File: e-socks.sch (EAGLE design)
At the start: 91 parts, among them IC1 CC2540, IC2 741G240DCK, IC3 TPS6300X, P2 TMAV433BAA, Q1 FA-20H(32MHz), Q2 ABS06, U2 MAX21000, X4 1296-T10

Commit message: erstes commit für diesen branch
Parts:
- removed C1: 100nF, rcl:C-EUC0402
- removed IC3: TPS6300X, m_vreg:TPS6300XDRC
- removed L1: CR32, inductors:CR32
- added LED3, LED4: Blue/2.9V@10mA, led:LEDCHIP-LED0603
- added R8: 47RR, rcl:R-EU_R0402
- C5, C6: value 10µF -> 22µF; device rcl:C-EUC0603 -> rcl:C-EUC0805
- R6: value 100R -> 47RR
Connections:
- removed net N$10: C1.2, IC3.!PS!/SYNC, IC3.VINA, R6.2
- net +5V: now also IC7.VOUT; no longer IC3.VOUT
- net 5V_ENABLE: now also IC7.EN; no longer IC3.EN
- net GND: now also LED3.C, LED4.C; no longer C1.1, IC3.GND, IC3.PGND
- net HEATER1_PWR: now also R8.1
- net HEATER2_PWR: now also R6.1
- net N$1: now also LED3.A, R6.2; no longer IC3.L1, L1.1
- net N$3: now also LED4.A, R8.2; no longer IC3.L2, L1.2
- net N$4: now also IC7.FB; no longer IC3.FB
- net VBAT: no longer IC3.VIN, R6.1
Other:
- moved on the sheet: C5, C6, C9, IC7, L3, R3, R5, R6

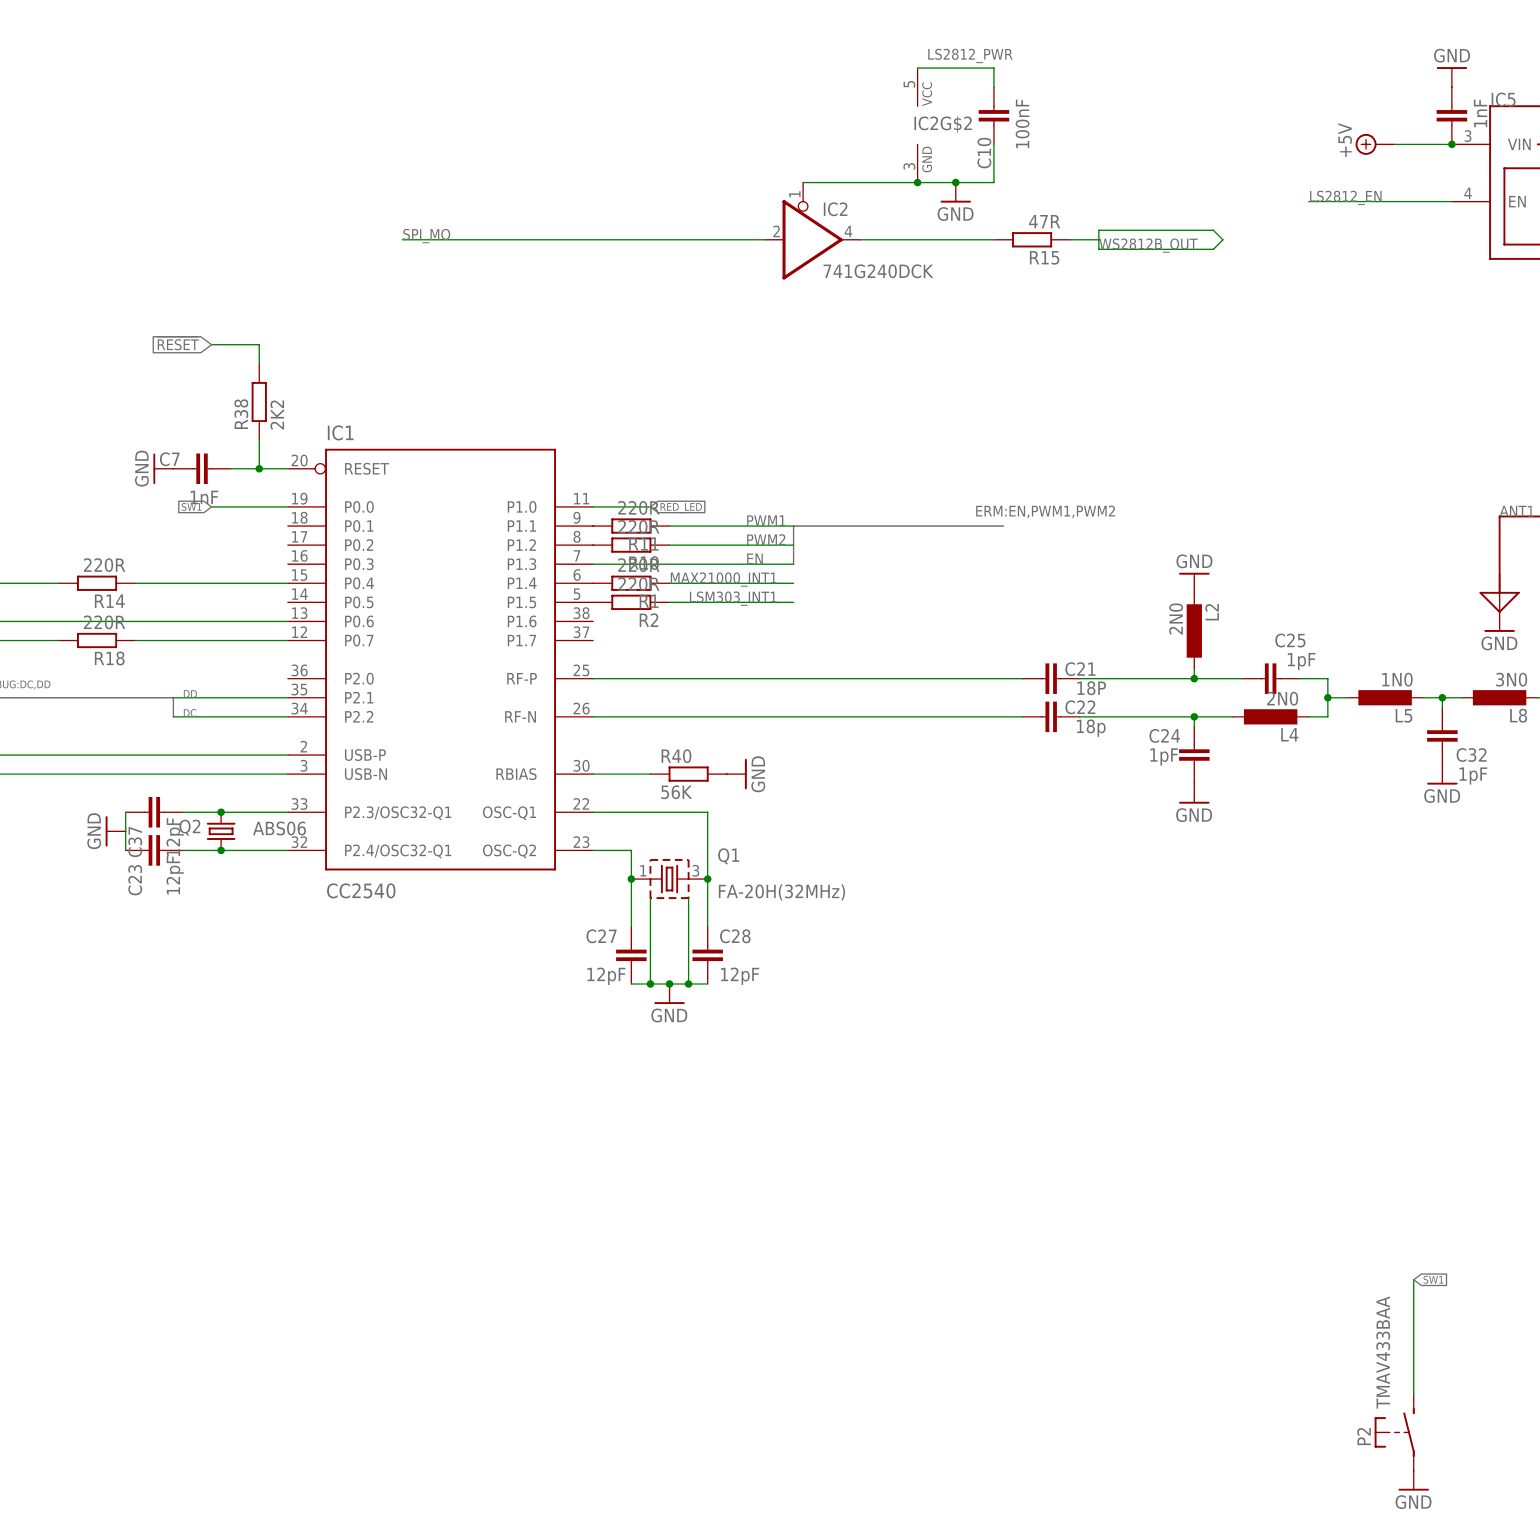
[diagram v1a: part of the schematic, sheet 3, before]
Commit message: taster getauscht, 2.5mm klinke hinzugefügt, noch nicht geroutet
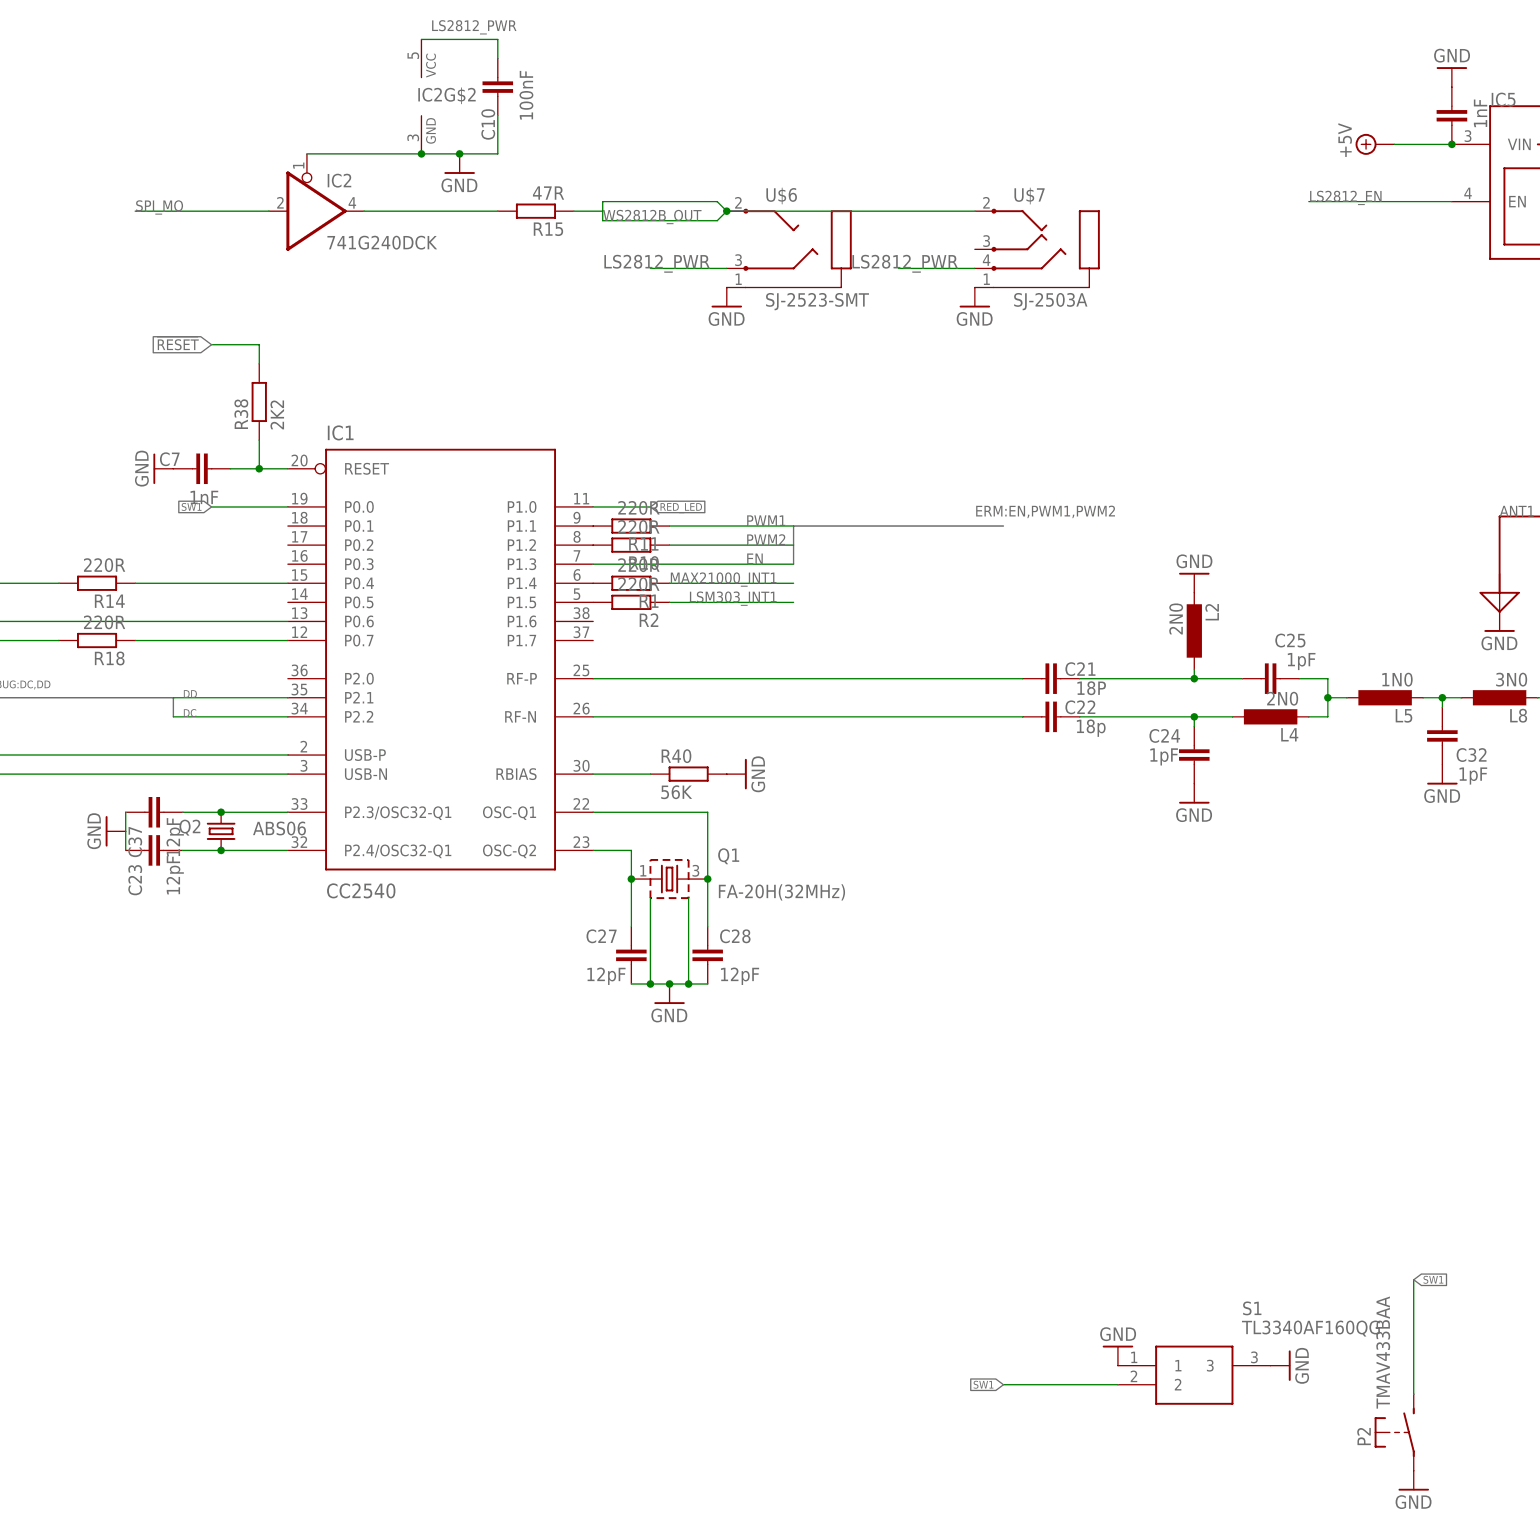
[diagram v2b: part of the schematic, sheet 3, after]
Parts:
- added S1: TL3340AF160QG, SamacSys_Parts:TL3340AF160QG
- added U$6: SJ-2523-SMT, con-cuistack:SJ-2523-SMT
- added U$7: SJ-2503A, con-cuistack:SJ-2503A
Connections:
- net GND: now also S1.1, S1.3, U$6.EARTH, U$7.1
- net LS2812_PWR: now also U$6.RING, U$7.4
- net SW1: now also S1.2
- net WS2812B_OUT: now also U$6.TIP, U$7.2
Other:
- moved on the sheet: C10, IC2, IC2G$2, R15

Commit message: routing fertig @home
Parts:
- removed P2: TMAV433BAA, switch-misc:TMAV433BAA
- removed U$6: SJ-2523-SMT, con-cuistack:SJ-2523-SMT
- added S2: TL3340AF160QG, SamacSys_Parts:TL3340AF160QG
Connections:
- removed net N$33: R4.2, U$1.CHRG
- new net !CHRG: IC1CC2540.P0.5, R4.2, U$1.CHRG
- new net SW2: IC1CC2540.P0.1, S2.2
- net GND: now also S2.1, S2.3, U$1.CHGEN, U$1.LDOEN; no longer P2.P, U$6.EARTH
- net LS2812_PWR: no longer U$6.RING
- net SW1: no longer P2.S
- net WS2812B_OUT: now also U$7.3; no longer U$6.TIP, U$7.2
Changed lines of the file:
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@@
 <part name="L8" library="rcl-2" deviceset="L-EU" device="L0402" value="3N0"/>
 <part name="V1" library="supply" deviceset="VDD" device=""/>
-<part name="P2" library="switch-misc" deviceset="TMAV433BAA" device=""/>
 <part name="FRAME2" library="frames" deviceset="DINA3_L" device=""/>
 <part name="C4" library="resistor" deviceset="C-EU" device="C0402" value="2,2µF"/>
@@
 <part name="GND34" library="supply1" deviceset="GND" device=""/>
 <part name="GND42" library="supply1" deviceset="GND" device=""/>
-<part name="U$6" library="con-cuistack" deviceset="SJ-2523" device="-SMT"/>
 <part name="GND55" library="supply1" deviceset="GND" device=""/>
 <part name="U$7" library="con-cuistack" deviceset="SJ-2503A" device=""/>
 <part name="GND60" library="supply1" deviceset="GND" device=""/>
+<part name="S2" library="SamacSys_Parts" deviceset="TL3340AF160QG" device=""/>
+<part name="GND61" library="supply1" deviceset="GND" device=""/>
+<part name="GND62" library="supply1" deviceset="GND" device=""/>
+<part name="GND63" library="supply1" deviceset="GND" device=""/>
 </parts>
 <sheets>
@@
 <instance part="U$3" gate="G$1" x="78.74" y="129.54"/>
 <instance part="SUPPLY2" gate="GND" x="104.14" y="116.84" rot="R90"/>
+<instance part="GND62" gate="1" x="181.61" y="130.81" rot="R270"/>
+<instance part="GND63" gate="1" x="181.61" y="128.27" rot="R270"/>
 </instances>
 <busses>
@@
 <pinref part="SUPPLY31" gate="GND" pin="GND"/>
 </segment>
+<segment>
+<pinref part="U$1" gate="G$1" pin="CHGEN"/>
+<pinref part="GND62" gate="1" pin="GND"/>
+</segment>
+<segment>
+<pinref part="U$1" gate="G$1" pin="LDOEN"/>
+<pinref part="GND63" gate="1" pin="GND"/>
+</segment>
 </net>
 <net name="VBAT" class="0">
@@
 </segment>
 </net>
-<net name="N$33" class="0">
+<net name="!CHRG" class="0">
 <segment>
 <pinref part="U$1" gate="G$1" pin="CHRG"/>
 <pinref part="R4" gate="G$1" pin="2"/>
 <wire x1="184.15" y1="135.89" x2="177.8" y2="135.89" width="0.1524" layer="91"/>
+<wire x1="177.8" y1="135.89" x2="156.21" y2="135.89" width="0.1524" layer="91"/>
+<junction x="177.8" y="135.89"/>
+<label x="156.21" y="135.89" size="1.778" layer="95"/>
 </segment>
 </net>
@@
 <instance part="C7" gate="G$1" x="149.86" y="198.12" smashed="yes" rot="R90">
 <attribute name="NAME" x="148.336" y="200.279" size="1.778" layer="95" rot="R180"/>
-<attribute name="VALUE" x="153.416" y="195.199" size="1.778" layer="96" rot="R180"/>
+<attribute name="VALUE" x="157.226" y="196.469" size="1.778" layer="96" rot="R180"/>
 </instance>
 <instance part="C12" gate="G$1" x="254" y="24.13" rot="R180"/>
@@
 <instance part="GND37" gate="1" x="34.29" y="148.59" rot="R90"/>
 <instance part="GND39" gate="1" x="334.01" y="62.23"/>
-<instance part="GND40" gate="1" x="312.42" y="62.23"/>
+<instance part="GND40" gate="1" x="295.91" y="63.5" rot="R90"/>
 <instance part="R45" gate="G$1" x="334.01" y="82.55" rot="R270"/>
 <instance part="Q1" gate="G$1" x="213.36" y="143.51" smashed="yes">
@@
 <instance part="L8" gate="G$1" x="323.85" y="167.64" rot="R90"/>
 <instance part="V1" gate="G$1" x="34.29" y="163.83" rot="R270"/>
-<instance part="P2" gate="G$1" x="312.42" y="69.85"/>
 <instance part="Q2" gate="Q" x="153.67" y="149.86" smashed="yes" rot="R90">
 <attribute name="NAME" x="151.13" y="151.384" size="1.778" layer="95" rot="R180"/>
@@
 <instance part="GND34" gate="1" x="295.91" y="78.74" rot="R90"/>
 <instance part="GND42" gate="1" x="273.05" y="81.28" rot="R180"/>
-<instance part="U$6" gate="G$1" x="233.68" y="229.87"/>
 <instance part="GND55" gate="1" x="220.98" y="219.71"/>
 <instance part="U$7" gate="SJ-2503A" x="266.7" y="229.87"/>
 <instance part="GND60" gate="1" x="254" y="219.71"/>
+<instance part="S2" gate="G$1" x="273.05" y="63.5"/>
+<instance part="GND61" gate="1" x="273.05" y="66.04" rot="R180"/>
 </instances>
 <busses>
@@
 </segment>
 <segment>
-<pinref part="GND40" gate="1" pin="GND"/>
-<pinref part="P2" gate="G$1" pin="P"/>
-</segment>
-<segment>
 <pinref part="C37" gate="G$1" pin="1"/>
 <pinref part="GND1" gate="1" pin="GND"/>
@@
 </segment>
 <segment>
-<pinref part="U$6" gate="G$1" pin="EARTH"/>
-<pinref part="GND55" gate="1" pin="GND"/>
-</segment>
-<segment>
 <pinref part="U$7" gate="SJ-2503A" pin="1"/>
 <pinref part="GND60" gate="1" pin="GND"/>
+</segment>
+<segment>
+<pinref part="S2" gate="G$1" pin="3"/>
+<pinref part="GND40" gate="1" pin="GND"/>
+</segment>
+<segment>
+<pinref part="S2" gate="G$1" pin="1"/>
+<pinref part="GND61" gate="1" pin="GND"/>
 </segment>
 </net>
@@
 <net name="SW1" class="0">
 <segment>
-<label x="312.42" y="90.17" size="1.016" layer="95" xref="yes"/>
-<label x="257.81" y="76.2" size="1.016" layer="95" rot="R180" xref="yes"/>
-</segment>
-<segment>
-<pinref part="P2" gate="G$1" pin="S"/>
-<wire x1="312.42" y1="74.93" x2="312.42" y2="90.17" width="0.1524" layer="91"/>
 <wire x1="273.05" y1="76.2" x2="257.81" y2="76.2" width="0.1524" layer="91"/>
 <pinref part="S1" gate="G$1" pin="2"/>
-</segment>
-<segment>
-<label x="152.4" y="193.04" size="1.016" layer="95" rot="R180" xref="yes"/>
+<label x="260.35" y="76.2" size="1.778" layer="95"/>
 </segment>
 <segment>
 <wire x1="162.56" y1="193.04" x2="152.4" y2="193.04" width="0.1524" layer="91"/>
 <pinref part="IC1" gate="CC2540" pin="P0.0"/>
+<label x="156.21" y="193.04" size="1.778" layer="95"/>
 </segment>
 </net>
@@
 <label x="204.47" y="231.14" size="1.4224" layer="95"/>
 <pinref part="R15" gate="G$1" pin="1"/>
-<pinref part="U$6" gate="G$1" pin="TIP"/>
 <junction x="220.98" y="232.41"/>
-<pinref part="U$7" gate="SJ-2503A" pin="2"/>
-<wire x1="254" y1="232.41" x2="220.98" y2="232.41" width="0.1524" layer="91"/>
+<pinref part="U$7" gate="SJ-2503A" pin="3"/>
+<wire x1="248.92" y1="232.41" x2="220.98" y2="232.41" width="0.1524" layer="91"/>
+<wire x1="254" y1="227.33" x2="248.92" y2="227.33" width="0.1524" layer="91"/>
+<wire x1="248.92" y1="227.33" x2="248.92" y2="232.41" width="0.1524" layer="91"/>
 </segment>
 </net>
@@
 <label x="193.04" y="257.81" size="1.4224" layer="95" rot="R180"/>
 <wire x1="210.82" y1="224.79" x2="220.98" y2="224.79" width="0.1524" layer="91"/>
-<pinref part="U$6" gate="G$1" pin="RING"/>
 <label x="204.47" y="224.79" size="1.778" layer="95"/>
 <wire x1="243.84" y1="224.79" x2="254" y2="224.79" width="0.1524" layer="91"/>
@@
 </segment>
 </net>
+<net name="SW2" class="0">
+<segment>
+<pinref part="IC1" gate="CC2540" pin="P0.1"/>
+<wire x1="162.56" y1="190.5" x2="152.4" y2="190.5" width="0.1524" layer="91"/>
+<label x="156.21" y="190.5" size="1.778" layer="95"/>
+<wire x1="273.05" y1="60.96" x2="262.89" y2="60.96" width="0.1524" layer="91"/>
+<pinref part="S2" gate="G$1" pin="2"/>
+<label x="262.89" y="60.96" size="1.778" layer="95"/>
+</segment>
+</net>
+<net name="!CHRG" class="0">
+<segment>
+<wire x1="162.56" y1="180.34" x2="140.97" y2="180.34" width="0.1524" layer="91"/>
+<label x="140.97" y="180.34" size="1.778" layer="95"/>
+<pinref part="IC1" gate="CC2540" pin="P0.5"/>
+</segment>
+</net>
